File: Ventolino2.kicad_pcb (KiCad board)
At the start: 2 copper layers, 85.1 x 52.1 mm, 37 parts, among them J1 Screw_Terminal_01x03, J2 Conn_01x10, J3 Conn_01x10, J4 Conn_01x10, J5 Conn_01x10, U1 MC78L12_TO92, U2 LM79L12_TO92, U3 MAX6225, U4 MAX525, U5 LM324

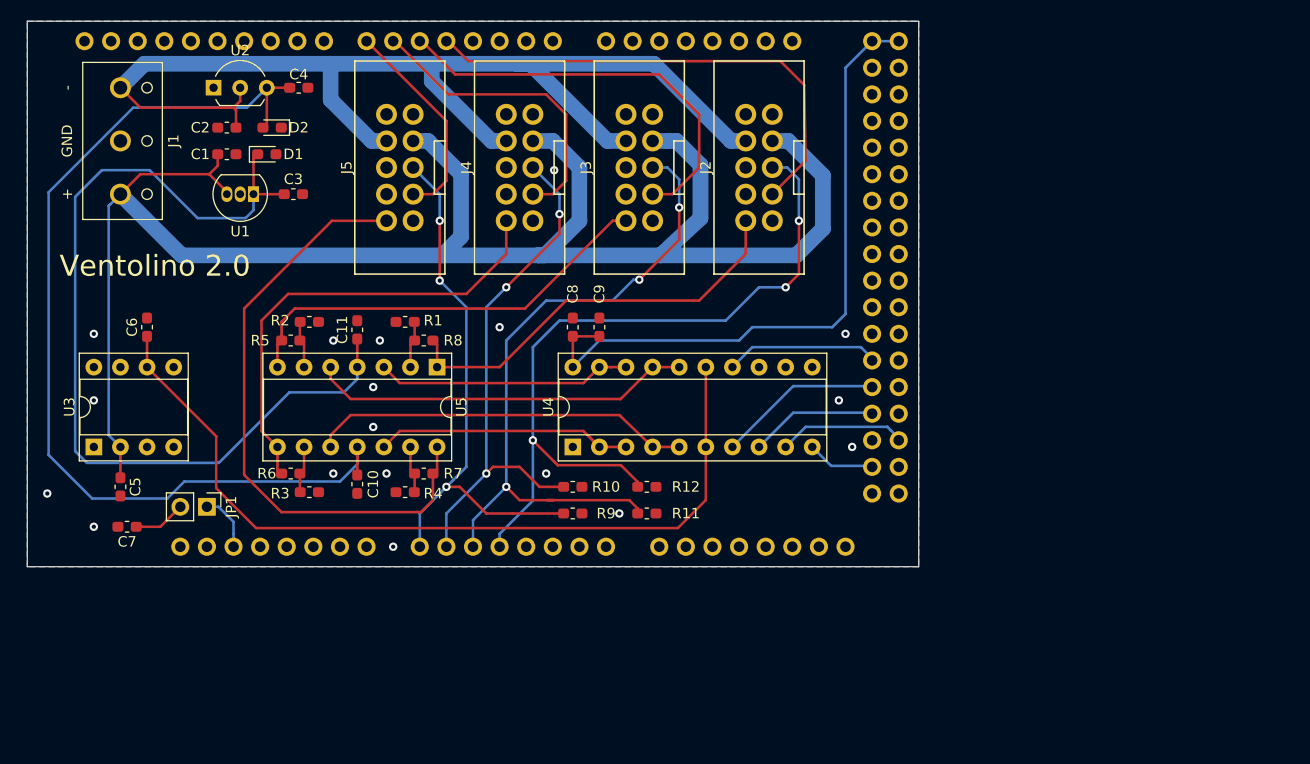
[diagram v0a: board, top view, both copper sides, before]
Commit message: Redrew PCB in the old KiCad Format for compatibility
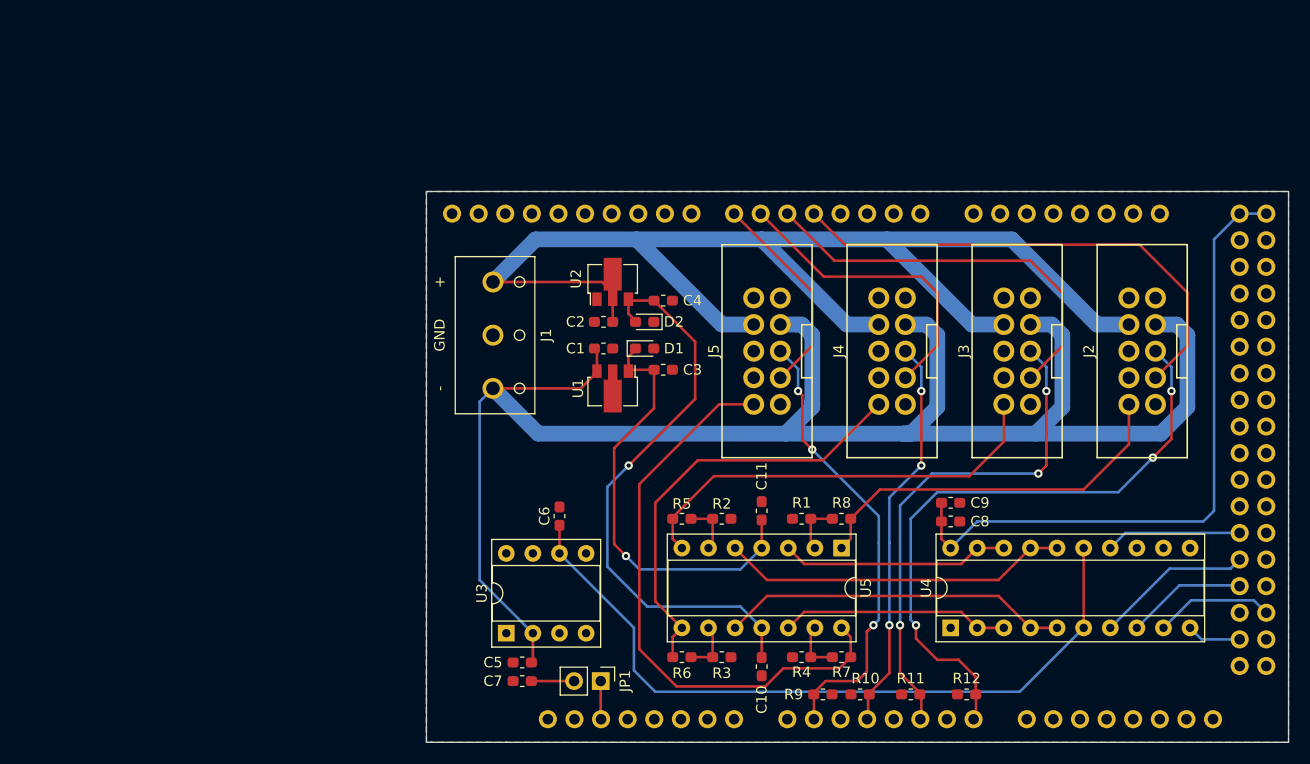
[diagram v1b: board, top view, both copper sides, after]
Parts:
- U1: value MC78L12_TO92 -> L78L12_SOT89; footprint Package_TO_SOT_THT:TO-92_Inline -> Package_TO_SOT_SMD:SOT-89-3
- U2: value LM79L12_TO92 -> L79L12_SOT89; footprint Package_TO_SOT_THT:TO-92L_Inline_Wide -> Package_TO_SOT_SMD:SOT-89-3
- moved R2 43.6 mm to (129.8, 103.4)
- moved R7 43.6 mm to (141.2, 116.6)
- moved R8 43.4 mm to (141.2, 103.4)
- moved C6 43.3 mm to (114.3, 103.1)
- moved U3 43.2 mm to (109.2, 114.3)
- moved R3 42.4 mm to (129.8, 116.6)
- moved U2 42.4 mm to (119.4, 80.8), turned to 90 degrees
- moved C10 42.4 mm to (133.6, 117.5)
- moved C11 42.3 mm to (133.6, 102.6)
- moved U5 42.3 mm to (141.2, 106.2)
- moved R1 42.3 mm to (137.4, 103.4)
- moved C5 41.9 mm to (110.7, 117.1), turned to 180 degrees
- moved R6 41.2 mm to (126.0, 116.6)
- moved JP1 41.1 mm to (118.2, 118.9)
- moved R5 41.0 mm to (126.0, 103.4)
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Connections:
- U3 pad 1: (no net) -> Net-(U3-Pad1)
- U3 pad 3: (no net) -> Net-(U3-Pad3)
- U3 pad 5: (no net) -> Net-(U3-Pad5)
- U3 pad 7: (no net) -> Net-(U3-Pad7)
- U3 pad 8: (no net) -> Net-(U3-Pad8)
- U4 pad 12: (no net) -> Net-(U4-Pad12)
- U4 pad 13: (no net) -> Net-(U4-Pad13)
- XA1 pad 3V3: (no net) -> Net-(XA1-Pad3V3)
- XA1 pad 5V1: (no net) -> Net-(XA1-Pad5V1)
- XA1 pad A0: Net-(J5-Pad5) -> Net-(XA1-PadA0)
- XA1 pad A1: Net-(J4-Pad5) -> Net-(J5-Pad5)
- XA1 pad A10: (no net) -> Net-(XA1-PadA10)
- XA1 pad A11: (no net) -> Net-(XA1-PadA11)
- XA1 pad A12: (no net) -> Net-(XA1-PadA12)
- XA1 pad A13: (no net) -> Net-(XA1-PadA13)
- XA1 pad A14: (no net) -> Net-(XA1-PadA14)
- XA1 pad A15: (no net) -> Net-(XA1-PadA15)
- XA1 pad A2: Net-(J3-Pad5) -> Net-(XA1-PadA2)
- XA1 pad A3: Net-(J2-Pad5) -> Net-(J4-Pad5)
- XA1 pad A4: (no net) -> Net-(XA1-PadA4)
- XA1 pad A5: (no net) -> Net-(J3-Pad5)
- XA1 pad A6: (no net) -> Net-(XA1-PadA6)
- XA1 pad A7: (no net) -> Net-(J2-Pad5)
- XA1 pad A8: (no net) -> Net-(XA1-PadA8)
- XA1 pad A9: (no net) -> Net-(XA1-PadA9)
- XA1 pad AREF: (no net) -> Net-(XA1-PadAREF)
- XA1 pad D0: (no net) -> Net-(XA1-PadD0)
- XA1 pad D1: (no net) -> Net-(XA1-PadD1)
- XA1 pad D10: (no net) -> Net-(XA1-PadD10)
- XA1 pad D11: (no net) -> Net-(XA1-PadD11)
- XA1 pad D12: (no net) -> Net-(XA1-PadD12)
- XA1 pad D13: (no net) -> Net-(XA1-PadD13)
- XA1 pad D14: (no net) -> Net-(XA1-PadD14)
- XA1 pad D15: (no net) -> Net-(XA1-PadD15)
- XA1 pad D16: (no net) -> Net-(XA1-PadD16)
- XA1 pad D17: (no net) -> Net-(XA1-PadD17)
- XA1 pad D18: (no net) -> Net-(XA1-PadD18)
- XA1 pad D19: (no net) -> Net-(XA1-PadD19)
- XA1 pad D2: (no net) -> Net-(XA1-PadD2)
- XA1 pad D20: (no net) -> Net-(XA1-PadD20)
- XA1 pad D21: (no net) -> Net-(XA1-PadD21)
- XA1 pad D22: (no net) -> Net-(XA1-PadD22)
- XA1 pad D23: (no net) -> Net-(XA1-PadD23)
- XA1 pad D24: (no net) -> Net-(XA1-PadD24)
- XA1 pad D25: (no net) -> Net-(XA1-PadD25)
- XA1 pad D26: (no net) -> Net-(XA1-PadD26)
- XA1 pad D27: (no net) -> Net-(XA1-PadD27)
- XA1 pad D28: (no net) -> Net-(XA1-PadD28)
- XA1 pad D29: (no net) -> Net-(XA1-PadD29)
- XA1 pad D3: (no net) -> Net-(XA1-PadD3)
- XA1 pad D30: (no net) -> Net-(XA1-PadD30)
- XA1 pad D31: (no net) -> Net-(XA1-PadD31)
- XA1 pad D32: (no net) -> Net-(XA1-PadD32)
- XA1 pad D33: (no net) -> Net-(XA1-PadD33)
- XA1 pad D34: (no net) -> Net-(XA1-PadD34)
- XA1 pad D35: (no net) -> Net-(XA1-PadD35)
- XA1 pad D36: (no net) -> Net-(XA1-PadD36)
- XA1 pad D37: (no net) -> Net-(XA1-PadD37)
- XA1 pad D38: (no net) -> Net-(XA1-PadD38)
- XA1 pad D39: (no net) -> Net-(XA1-PadD39)
- XA1 pad D40: (no net) -> Net-(XA1-PadD40)
- XA1 pad D41: (no net) -> Net-(XA1-PadD41)
- XA1 pad D42: (no net) -> Net-(XA1-PadD42)
- XA1 pad D43: (no net) -> Net-(XA1-PadD43)
- XA1 pad D45: (no net) -> Net-(XA1-PadD45)
- XA1 pad D47: (no net) -> Net-(XA1-PadD47)
- XA1 pad D49: (no net) -> Net-(XA1-PadD49)
- XA1 pad D50: (no net) -> Net-(XA1-PadD50)
- XA1 pad D53: (no net) -> Net-(XA1-PadD53)
- XA1 pad D8: (no net) -> Net-(XA1-PadD8)
- XA1 pad D9: (no net) -> Net-(XA1-PadD9)
- XA1 pad IORF: (no net) -> Net-(XA1-PadIORF)
- XA1 pad SCL: (no net) -> Net-(XA1-PadSCL)
- XA1 pad SDA: (no net) -> Net-(XA1-PadSDA)
- XA1 pad VIN: (no net) -> Net-(XA1-PadVIN)
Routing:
- net +12V: track 87.5 -> 41.7 mm, vias 0 -> 1
- net -12V: track 93.5 -> 55.9 mm, vias 0 -> 1
- net Net-(J3-Pad5): track 64.7 -> 48.3 mm
- net Net-(J4-Pad5): track 50.2 -> 37.8 mm
- net Net-(J2-Pad5): track 72.8 -> 60.9 mm
- net -VDC: track 114.5 -> 123.5 mm
- net Net-(J5-Pad5): track 52.4 -> 43.4 mm
- net +2V5: track 79.3 -> 70.7 mm
- net +VDC: track 170.0 -> 164.5 mm
- net Net-(U4-Pad2): track 26.0 -> 21.8 mm
- net Net-(J2-Pad2): track 39.8 -> 36.5 mm
- net Net-(U4-Pad16): track 36.5 -> 33.3 mm
- net Net-(J4-Pad2): track 44.6 -> 41.4 mm
- net Net-(U4-Pad4): track 36.4 -> 33.3 mm
- net Net-(J5-Pad2): track 58.6 -> 55.8 mm
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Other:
- board size 85.1 x 52.1 mm -> 82.3 x 52.6 mm
- board text removed: "Ventolino 2.0"
